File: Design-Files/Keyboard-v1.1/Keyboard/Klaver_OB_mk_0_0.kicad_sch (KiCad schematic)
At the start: 254 parts, among them CN1 PJ-399F-6A, CN2 PJ-399F-6A, J1 TYPE-C-31-M-13C, J3 Conn_01x04, J4 Conn_01x03, J5 TYPE-C-31-M-13C, J7 Conn_01x04, J8 Conn_01x03, U1 RP2040, U2 NCP1117LPST33T3G, U3 TPD4E05U06DQAR, U4 W25Q128JVSIQ, U5 TPD4E05U06DQAR, U6 W25Q128JVSIQ, U7 NCP1117LPST33T3G, U8 RP2040, Y1 12MHz 18pF, Y2 12MHz 18pF

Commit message: #3 added resistors on i2c bus added tvs diodes and on data bus for addressable leds
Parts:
- removed D1: 1N4148WT, Diode_SMD:D_SOD-523, symbol Library:1N4148WT
- added D3: ~, SMBJ5.0:DIOM4336X265N, symbol SMBJ5.0:SMBJ5.0
- added R15, R16, R17: 1k, Resistor_SMD:R_0402_1005Metric, symbol Library:R
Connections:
- net +3V3_0: now also R15.1, R17.1
- net +5V_0: now also EXLED1.1 (VDD), EXLED2.1 (VDD), LED1.1 (VDD), LED10.1 (VDD), LED11.1 (VDD), LED12.1 (VDD), LED13.1 (VDD), LED14.1 (VDD), LED15.1 (VDD), LED16.1 (VDD), LED17.1 (VDD), LED18.1 (VDD), LED19.1 (VDD), LED2.1 (VDD), LED20.1 (VDD), LED21.1 (VDD), LED3.1 (VDD), LED4.1 (VDD), LED5.1 (VDD), LED6.1 (VDD), LED7.1 (VDD), LED8.1 (VDD), LED9.1 (VDD), D3.C
- net GND_0: now also D3.A
- net LED_0: now also R16.1; no longer LED21.4 (DIN)
- net SCL_0: now also R15.2
- net SDA_0: now also R17.2
- new net: LED21.4 (DIN), R16.2

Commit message: #3 done all changes in schematic except placement of sata connector
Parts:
- removed D2: 1N4148WT, Diode_SMD:D_SOD-523, symbol Library:1N4148WT
- removed D3: ~, SMBJ5.0:DIOM4336X265N, symbol SMBJ5.0:SMBJ5.0
- removed ZD1: ESD5Z5V0C, Diode_SMD:D_SOD-523, symbol Library:ESD5Zxx
- added C33, C34, C35, C36, C37, C38, C39, C40, C41, C42, C43, C44, C45, C46, C47, C48, C49, C50, C51, C52, C53, C54, C55, C56, C57, C58, C59, C60, C61, C62, C63, C64, C65, C66, C67, C68, C69, C70, C71, C72, C73, C74, C75, C76, C77, C78: 100n, Capacitor_SMD:C_0402_1005Metric, symbol Library:C_Small
- added D1, D2: ESD9B5.0ST5G, Diode_SMD:D_SOD-923, symbol Diode:ESD9B5.0ST5G
- added F3: BSMD0603-050-12V, Fuse:Fuse_0603_1608Metric, symbol Library:Fuse
- added F4: BSMD0805L-150, Fuse:Fuse_0805_2012Metric, symbol Library:Fuse
- added J2, J6: 5607-4200-SH, 5607-4200-SH:3M_5607-4200-SH, symbol 5607-4200-SH:5607-4200-SH
- added Q1, Q2: BSS138, Package_TO_SOT_SMD:SOT-23, symbol Transistor_FET:BSS138
- added R18: 499R, Resistor_SMD:R_0402_1005Metric, symbol Library:R
- added R19, R20, R21, R22, R23, R24, R25, R26, R27, R28, R29, R30, R31, R32, R33, R34, R35, R36: 1k, Resistor_SMD:R_0402_1005Metric, symbol Library:R
- F1: value BSMD0603-050-12V -> BSMD0805L-150; footprint Fuse:Fuse_0603_1608Metric -> Fuse:Fuse_0805_2012Metric; JLCPCB Part # C2844464 -> C914095
- R16: value 1k -> 499R
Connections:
- net +3V3: now also C34.1, R19.1, R20.1, R32.2, R35.2
- net +3V3_0: now also C33.1, R31.2, R34.2
- net +5V: now also EXLED3.1 (VDD), EXLED4.1 (VDD), LED22.1 (VDD), LED23.1 (VDD), LED24.1 (VDD), LED25.1 (VDD), LED26.1 (VDD), LED27.1 (VDD), LED28.1 (VDD), LED29.1 (VDD), LED30.1 (VDD), LED31.1 (VDD), LED32.1 (VDD), LED33.1 (VDD), LED34.1 (VDD), LED35.1 (VDD), LED36.1 (VDD), LED37.1 (VDD), LED38.1 (VDD), LED39.1 (VDD), LED40.1 (VDD), LED41.1 (VDD), LED42.1 (VDD), C57.1, C58.1, C59.1, C60.1, C61.1, C62.1, C63.1, C64.1, C65.1, C66.1, C67.1, C68.1, C69.1, C70.1, C71.1, C72.1, C73.1, C74.1, C75.1, C76.1, C77.1, C78.1, D2.2 (A2), F4.2, R36.2; no longer F2.2
- net +5V_0: now also C35.1, C36.1, C37.1, C38.1, C39.1, C40.1, C41.1, C42.1, C43.1, C44.1, C45.1, C46.1, C47.1, C48.1, C49.1, C50.1, C51.1, C52.1, C53.1, C54.1, C55.1, C56.1, D1.2 (A2), R33.2
- net GND: now also C34.2, C57.2, C58.2, C59.2, C60.2, C61.2, C62.2, C63.2, C64.2, C65.2, C66.2, C67.2, C68.2, C69.2, C70.2, C71.2, C72.2, C73.2, C74.2, C75.2, C76.2, C77.2, C78.2, R21.1, R22.1, R23.1, R24.1, R25.1; no longer ZD2.2 (A)
- net GND_0: now also C33.2, C35.2, C36.2, C37.2, C38.2, C39.2, C40.2, C41.2, C43.2, C44.2, C45.2, C46.2, C47.2, C48.2, C49.2, C50.2, C51.2, C52.2, C53.2, C54.2, C55.2, C56.2, D1.1 (A1), D2.1 (A1), R26.1, R27.1, R28.1, R29.1, R30.1
- net LED: now also Q2.3 (D), R18.1, R36.1; no longer LED42.4 (DIN), U8.17 (GPIO14)
- net LED_0: now also Q1.3 (D), R33.1; no longer U1.17 (GPIO14)
- net Row 0_0: now also R26.2
- net Row 0_1: now also R27.2
- net Row 0_2: now also R28.2
- net Row 0_3: now also R29.2
- net Row 0_4: now also R30.2
- net Row 1_0: now also R21.2
- net Row 1_1: now also R22.2
- net Row 1_2: now also R23.2
- net Row 1_3: now also R24.2
- net Row 1_4: now also R25.2
- net SCL: now also R19.2
- net SDA: now also R20.2
- net VBUS: now also F4.1; no longer F2.1, ZD2.1 (K)
- net at SMDSW1.2, U1.26 (RUN): now also R31.1
- net at SMDSW4.2, U8.26 (RUN): now also R32.1
- new net: J2.8 (SHIELD), J2.9 (SHIELD)
- new net: Q1.1 (G), Q1.2 (S), R34.1, U1.17 (GPIO14)
- new net: LED42.4 (DIN), R18.2
- new net: Q2.1 (G), Q2.2 (S), R35.1, U8.17 (GPIO14)
- new net: J6.8 (SHIELD), J6.9 (SHIELD)
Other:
- moved on the sheet: EXLED1, EXLED2, EXLED3, EXLED4, F2, LED1, LED10, LED11, LED12, LED13, LED14, LED15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

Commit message: #3 all schematic changes done
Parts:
- removed CN1, CN2: PJ-399F-6A, easyeda2kicad:AUDIO-SMD_PJ-399F-6A, symbol Library:PJ-399F-6A
- removed F2, F3: BSMD0603-050-12V, Fuse:Fuse_0603_1608Metric, symbol Library:Fuse
- removed J2, J6: 5607-4200-SH, 5607-4200-SH:3M_5607-4200-SH, symbol 5607-4200-SH:5607-4200-SH
- removed ZD2: ESD5Z5V0C, Diode_SMD:D_SOD-523, symbol Library:ESD5Zxx
- added sata1, sata2: 0470804002-1, sata molex 2:sata molex1, symbol 5607-4200-SH:0470804002new
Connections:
- net +5V: now also sata2.1, sata2.2
- net +5V_0: now also sata1.1, sata1.2
- net GND: now also sata2.3, sata2.4
- net GND_0: now also sata1.3, sata1.4
- net RX: now also sata2.6
- net RX_0: now also sata1.6
- net TX: now also sata2.5
- net TX_0: now also sata1.5
- no-connect marks 36 -> 32
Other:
- note removed: "T(4,5), R1(3), R2(2), S(1)"
- note removed: "TRRS"
- note removed: "left 3:RX_0, 4:TX_0 right 3:TX_0, 4:RX_0"
- moved on the sheet: C33

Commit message: #3
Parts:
- removed sata2: 0470804002-1, sata molex 2:sata molex1, symbol 5607-4200-SH:0470804002new
- added sata3: 0470804002-1, sata molex 2:sata molex1, symbol 5607-4200-SH:0470804002new
- sata1: JLCPCB Part # C20847970 -> (none); JLCPCB Part #  (none) -> C20847970
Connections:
- net +5V: now also sata1.1, sata1.2
- net +5V_0: now also sata3.1, sata3.2; no longer sata1.1, sata1.2
- net GND: now also sata1.3, sata1.4
- net GND_0: now also sata3.3, sata3.4; no longer sata1.3, sata1.4
- net RX: now also sata1.6
- net RX_0: now also sata3.6; no longer sata1.6
- net TX: now also sata1.5
- net TX_0: now also sata3.5; no longer sata1.5

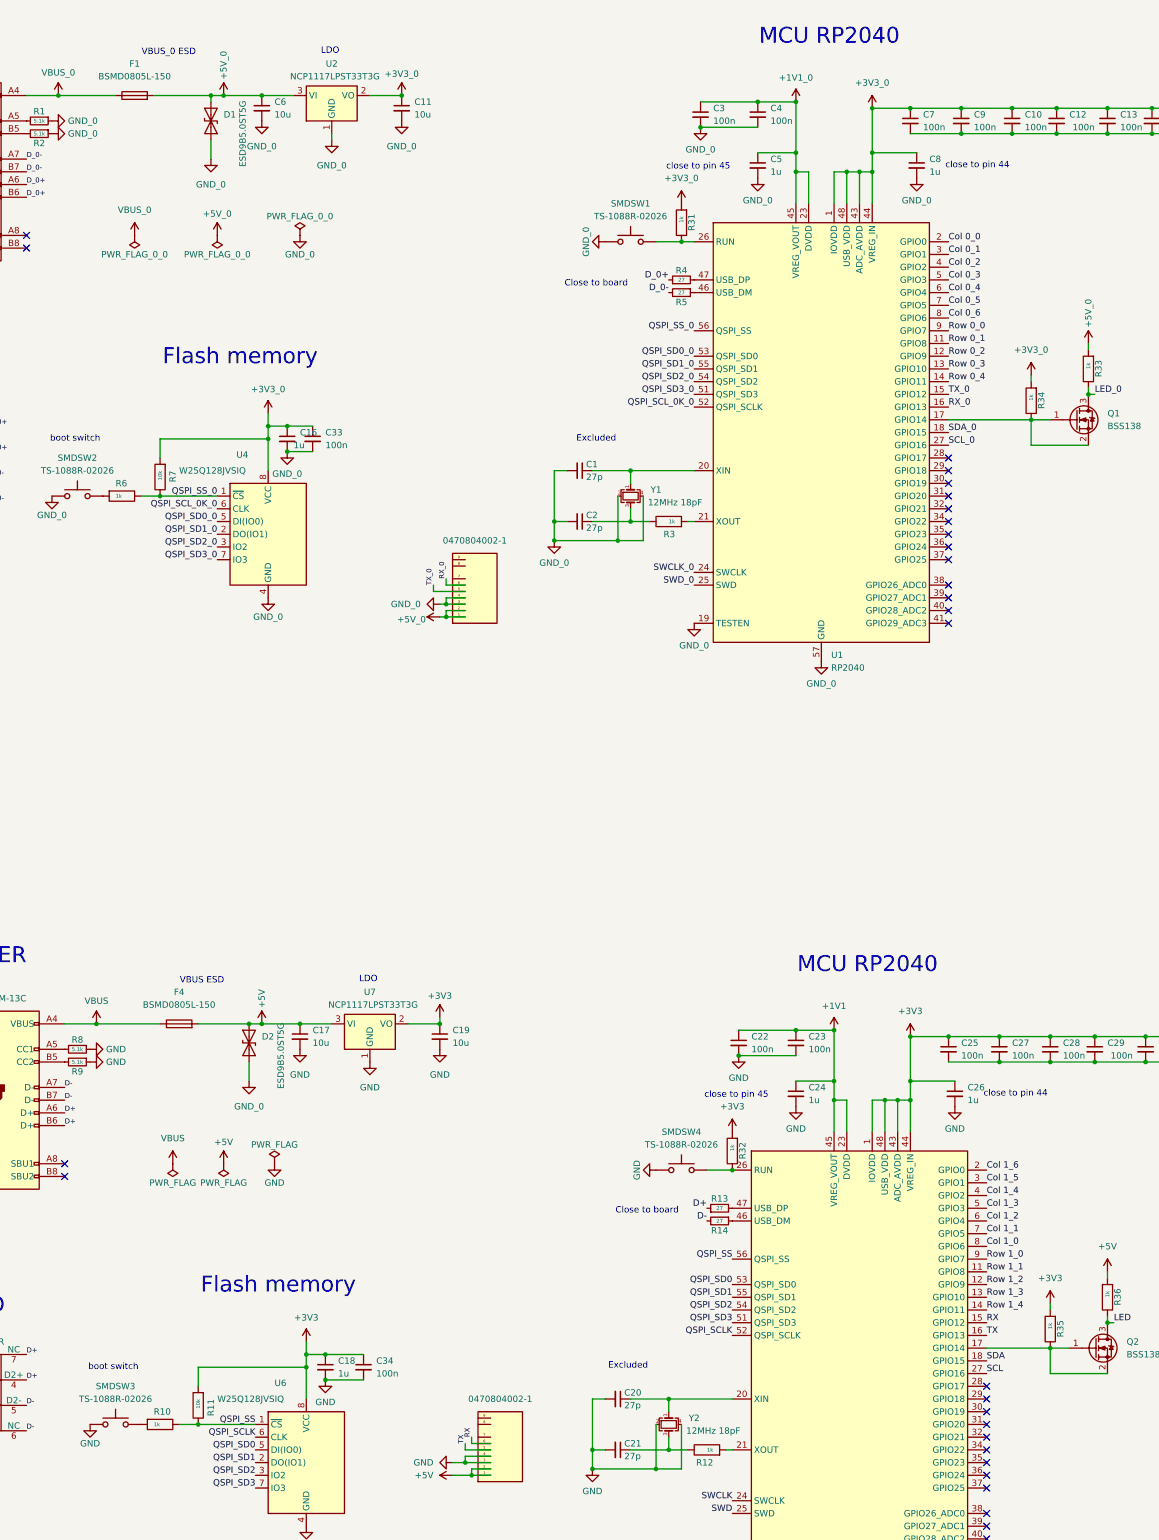
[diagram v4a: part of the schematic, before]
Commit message: #3 swaped TX RX, Fuse updated
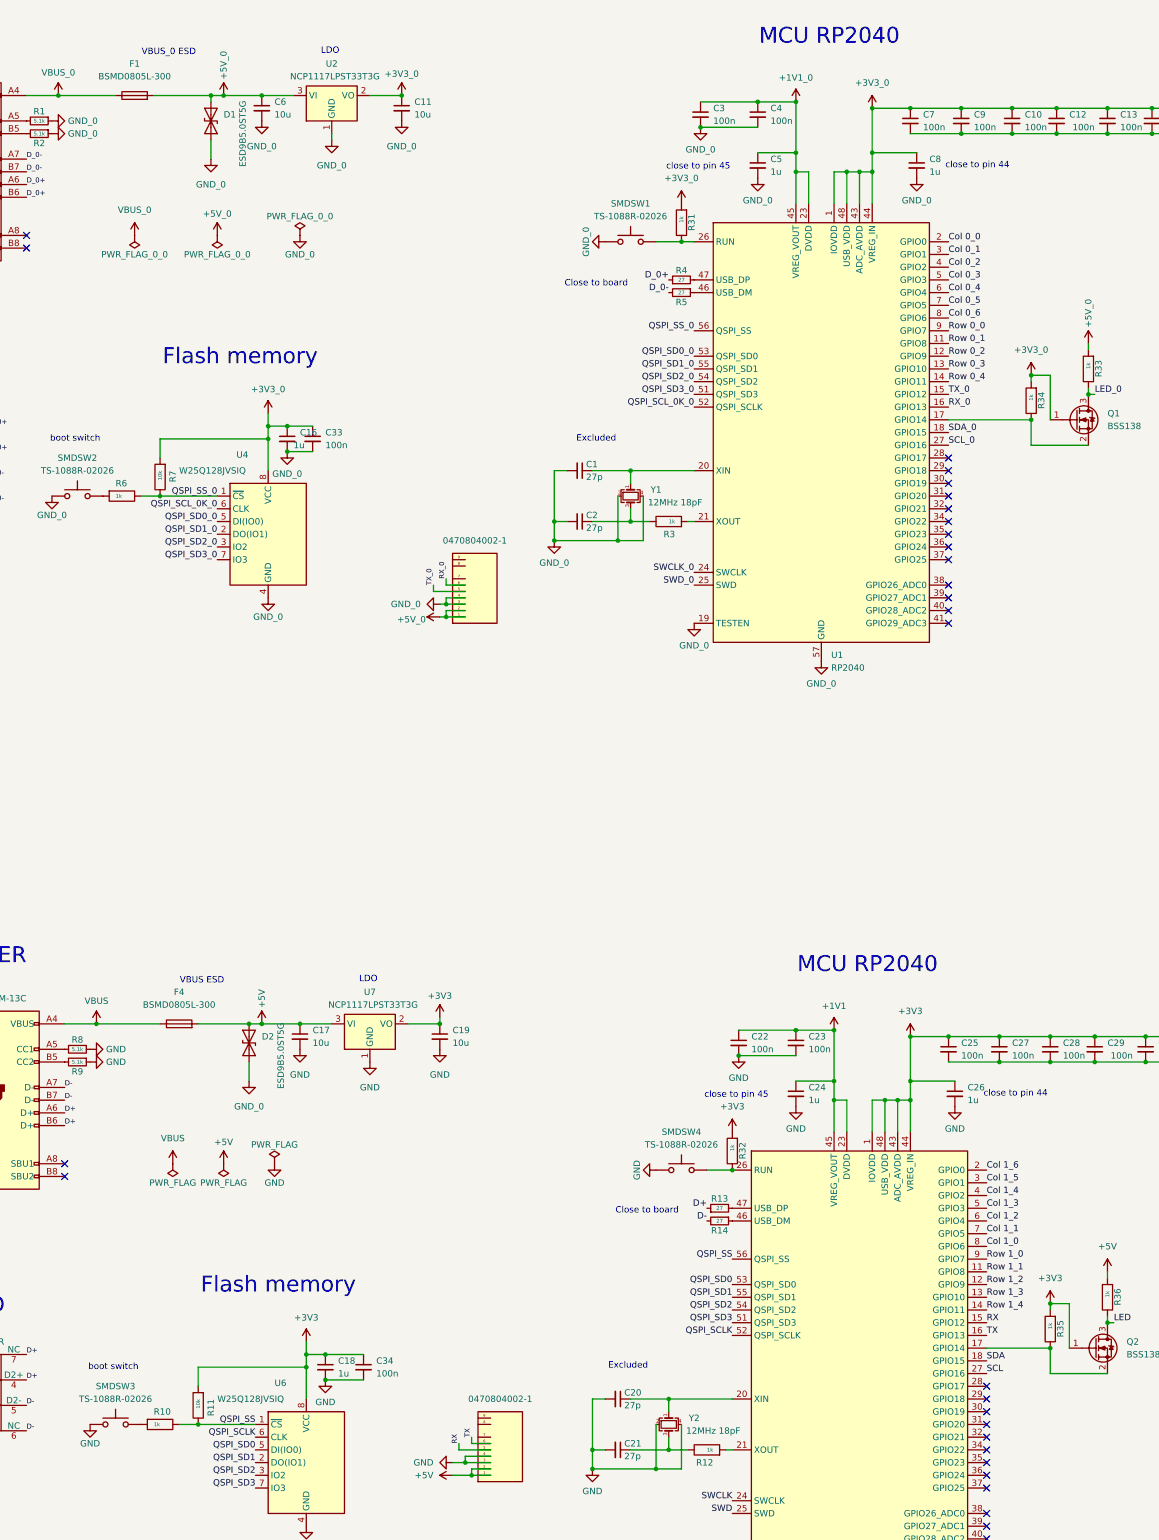
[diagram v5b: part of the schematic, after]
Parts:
- F1, F4: value BSMD0805L-150 -> BSMD0805L-300; JLCPCB Part # C914095 -> C2757932
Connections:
- net +3V3: now also Q2.1 (G)
- net +3V3_0: now also Q1.1 (G)
- net RX: now also sata1.5; no longer sata1.6
- net TX: now also sata1.6; no longer sata1.5
- net at Q1.2 (S), R34.1, U1.17 (GPIO14): no longer Q1.1 (G)
- net at Q2.2 (S), R35.1, U8.17 (GPIO14): no longer Q2.1 (G)
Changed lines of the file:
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@@
 	)
 	(junction
+		(at 264.16 275.59)
+		(diameter 0)
+		(color 0 0 0 0)
+	)
+	(junction
 		(at 383.54 83.82)
 		(diameter 0)
@@
 	)
 	(junction
+		(at 260.35 90.17)
+		(diameter 0)
+		(color 0 0 0 0)
+	)
+	(junction
 		(at 273.05 227.33)
 		(diameter 0)
@@
 	(wire
 		(pts
-			(xy 260.35 99.06) (xy 264.16 99.06)
-		)
-		(stroke
-			(width 0)
-			(type default)
-		)
-	)
-	(wire
-		(pts
 			(xy 345.44 299.72) (xy 358.14 299.72)
 		)
@@
 	(wire
 		(pts
+			(xy 267.97 275.59) (xy 267.97 284.48)
+		)
+		(stroke
+			(width 0)
+			(type default)
+		)
+	)
+	(wire
+		(pts
 			(xy 546.1 323.85) (xy 556.26 323.85)
 		)
@@
 	(wire
 		(pts
+			(xy 148.59 303.53) (xy 148.59 302.26)
+		)
+		(stroke
+			(width 0)
+			(type default)
+		)
+	)
+	(wire
+		(pts
 			(xy 530.86 297.18) (xy 530.86 309.88)
 		)
@@
 	(wire
 		(pts
-			(xy 264.16 284.48) (xy 267.97 284.48)
-		)
-		(stroke
-			(width 0)
-			(type default)
-		)
-	)
-	(wire
-		(pts
 			(xy 361.95 334.01) (xy 361.95 336.55)
 		)
@@
 	(wire
 		(pts
+			(xy 264.16 90.17) (xy 260.35 90.17)
+		)
+		(stroke
+			(width 0)
+			(type default)
+		)
+	)
+	(wire
+		(pts
 			(xy 480.06 224.79) (xy 480.06 242.57)
 		)
@@
 	(wire
 		(pts
-			(xy 147.32 304.8) (xy 152.4 304.8)
-		)
-		(stroke
-			(width 0)
-			(type default)
-		)
-	)
-	(wire
-		(pts
 			(xy 228.6 49.53) (xy 226.06 49.53)
 		)
@@
 	(wire
 		(pts
-			(xy 148.59 303.53) (xy 152.4 303.53)
-		)
-		(stroke
-			(width 0)
-			(type default)
-		)
-	)
-	(wire
-		(pts
 			(xy 327.66 96.52) (xy 327.66 118.11)
 		)
@@
 	(wire
 		(pts
+			(xy 264.16 275.59) (xy 267.97 275.59)
+		)
+		(stroke
+			(width 0)
+			(type default)
+		)
+	)
+	(wire
+		(pts
 			(xy 256.54 41.91) (xy 265.43 41.91)
 		)
@@
 	(wire
 		(pts
+			(xy 264.16 99.06) (xy 264.16 90.17)
+		)
+		(stroke
+			(width 0)
+			(type default)
+		)
+	)
+	(wire
+		(pts
 			(xy 378.46 261.62) (xy 378.46 287.02)
 		)
@@
 	(wire
 		(pts
-			(xy 148.59 302.26) (xy 148.59 303.53)
-		)
-		(stroke
-			(width 0)
-			(type default)
-		)
-	)
-	(wire
-		(pts
 			(xy 378.46 96.52) (xy 378.46 118.11)
 		)
@@
 	(wire
 		(pts
+			(xy 146.05 304.8) (xy 152.4 304.8)
+		)
+		(stroke
+			(width 0)
+			(type default)
+		)
+	)
+	(wire
+		(pts
 			(xy 548.64 242.57) (xy 548.64 261.62)
 		)
@@
 	(wire
 		(pts
-			(xy 147.32 303.53) (xy 147.32 304.8)
+			(xy 187.96 304.8) (xy 187.96 302.26)
 		)
 		(stroke
@@
 	(wire
 		(pts
-			(xy 187.96 304.8) (xy 187.96 302.26)
+			(xy 513.08 247.65) (xy 515.62 247.65)
 		)
 		(stroke
@@
 	(wire
 		(pts
-			(xy 513.08 247.65) (xy 515.62 247.65)
+			(xy 106.68 34.29) (xy 113.03 34.29)
 		)
 		(stroke
@@
 	(wire
 		(pts
-			(xy 106.68 34.29) (xy 113.03 34.29)
+			(xy 146.05 303.53) (xy 146.05 304.8)
 		)
 		(stroke
@@
 	(wire
 		(pts
+			(xy 152.4 303.53) (xy 148.59 303.53)
+		)
+		(stroke
+			(width 0)
+			(type default)
+		)
+	)
+	(wire
+		(pts
 			(xy 425.45 287.02) (xy 425.45 336.55)
 		)
@@
 	)
 	(label "RX"
-		(at 148.59 302.26 90)
+		(at 146.05 303.53 90)
 		(fields_autoplaced yes)
 		(effects
@@
 	)
 	(label "TX"
-		(at 147.32 303.53 90)
+		(at 148.59 302.26 90)
 		(fields_autoplaced yes)
 		(effects
@@
 			)
 		)
-		(property "Value" "BSMD0805L-150"
+		(property "Value" "BSMD0805L-300"
 			(at 90.17 215.9 90)
 			(effects
@@
 			)
 		)
-		(property "Datasheet" "~"
+		(property "Datasheet" "https://www.lcsc.com/datasheet/lcsc_datasheet_2305121425_BHFUSE-BSMD0805L-300_C2757932.pdf"
 			(at 90.17 219.71 0)
 			(effects
@@
 			)
 		)
-		(property "Description" "6V 1.5A 50A 3A 0805 Resettable Fuses ROHS"
+		(property "Description" "6V 3A 50A 6A 0805 Resettable Fuses ROHS"
 			(at 90.17 219.71 0)
 			(effects
@@
 			)
 		)
-		(property "JLCPCB Part #" "C914095"
+		(property "JLCPCB Part #" "C2757932"
 			(at 90.17 219.71 90)
 			(effects
@@
 			)
 		)
-		(property "Value" "BSMD0805L-150"
+		(property "Value" "BSMD0805L-300"
 			(at 81.28 30.48 90)
 			(effects
@@
 			)
 		)
-		(property "Datasheet" "~"
+		(property "Datasheet" "https://www.lcsc.com/datasheet/lcsc_datasheet_2305121425_BHFUSE-BSMD0805L-300_C2757932.pdf"
 			(at 81.28 34.29 0)
 			(effects
@@
 			)
 		)
-		(property "Description" "6V 1.5A 50A 3A 0805 Resettable Fuses ROHS"
+		(property "Description" "6V 3A 50A 6A 0805 Resettable Fuses ROHS"
 			(at 81.28 34.29 0)
 			(effects
@@
 			)
 		)
-		(property "JLCPCB Part #" "C914095"
+		(property "JLCPCB Part #" "C2757932 "
 			(at 81.28 34.29 90)
 			(effects
